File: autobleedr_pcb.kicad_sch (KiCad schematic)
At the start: 20 parts, among them J11 Conn_01x02_Pin, J13 Screw_Terminal_01x08, J7 Screw_Terminal_01x02, Q1 PMOS, Q2 IRLML2060, SW1 SW_SPST, U2 ESP32, U6 TMC2209

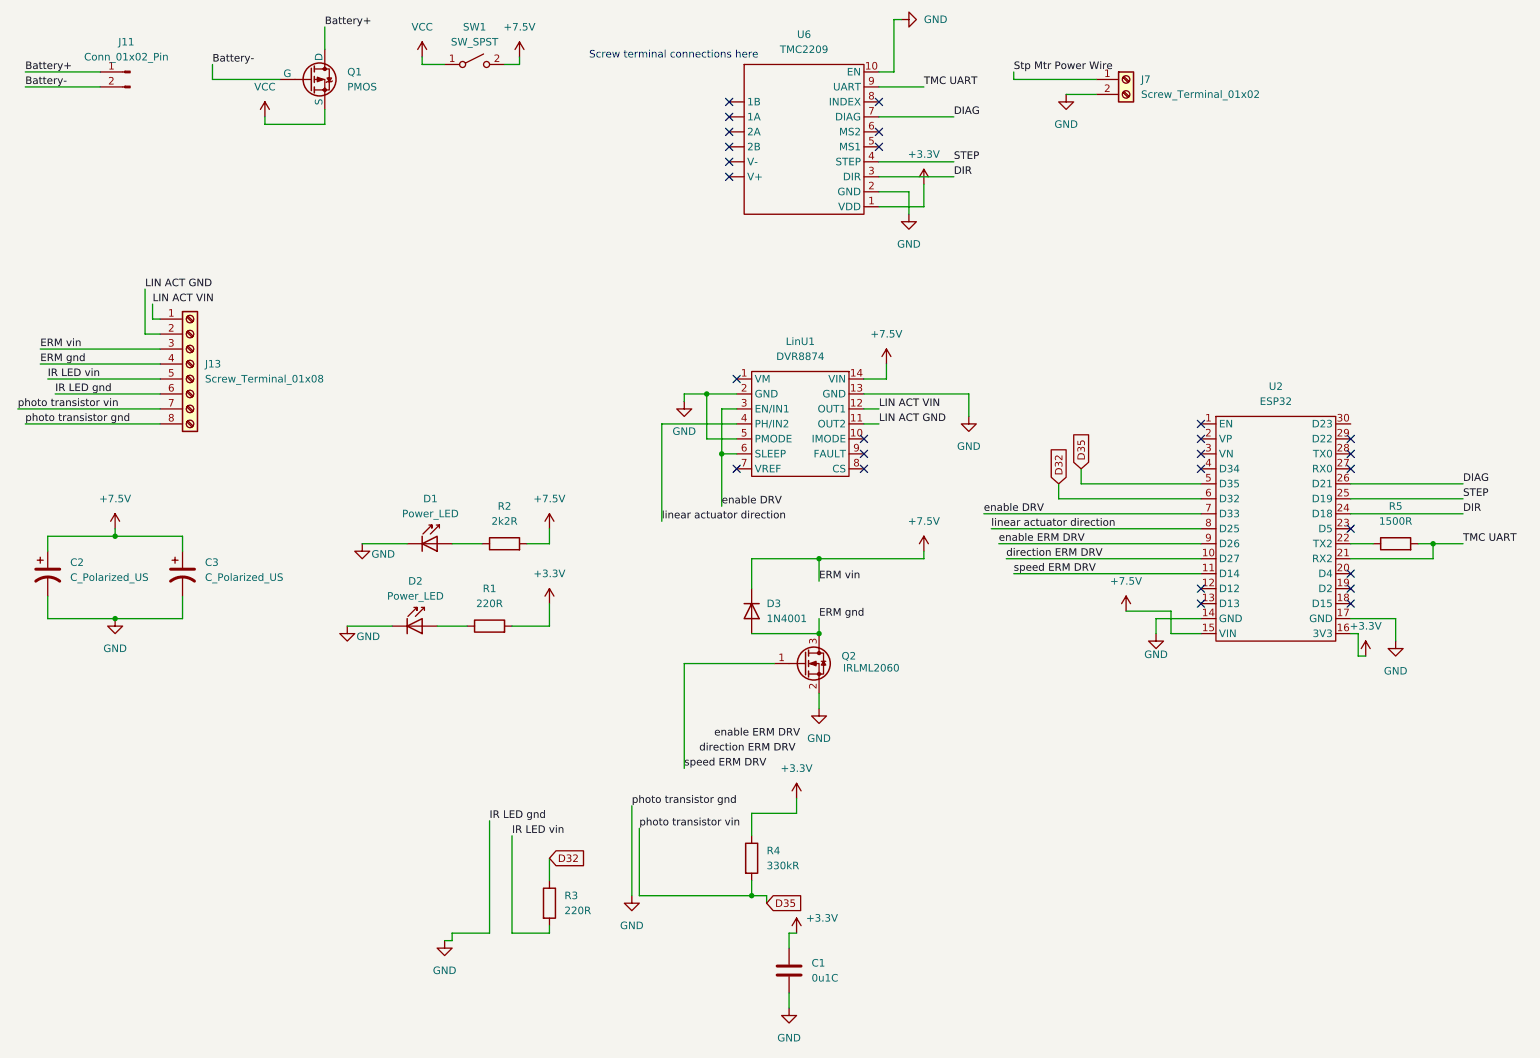
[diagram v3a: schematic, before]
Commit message: updated pcb traces with binh nmos design
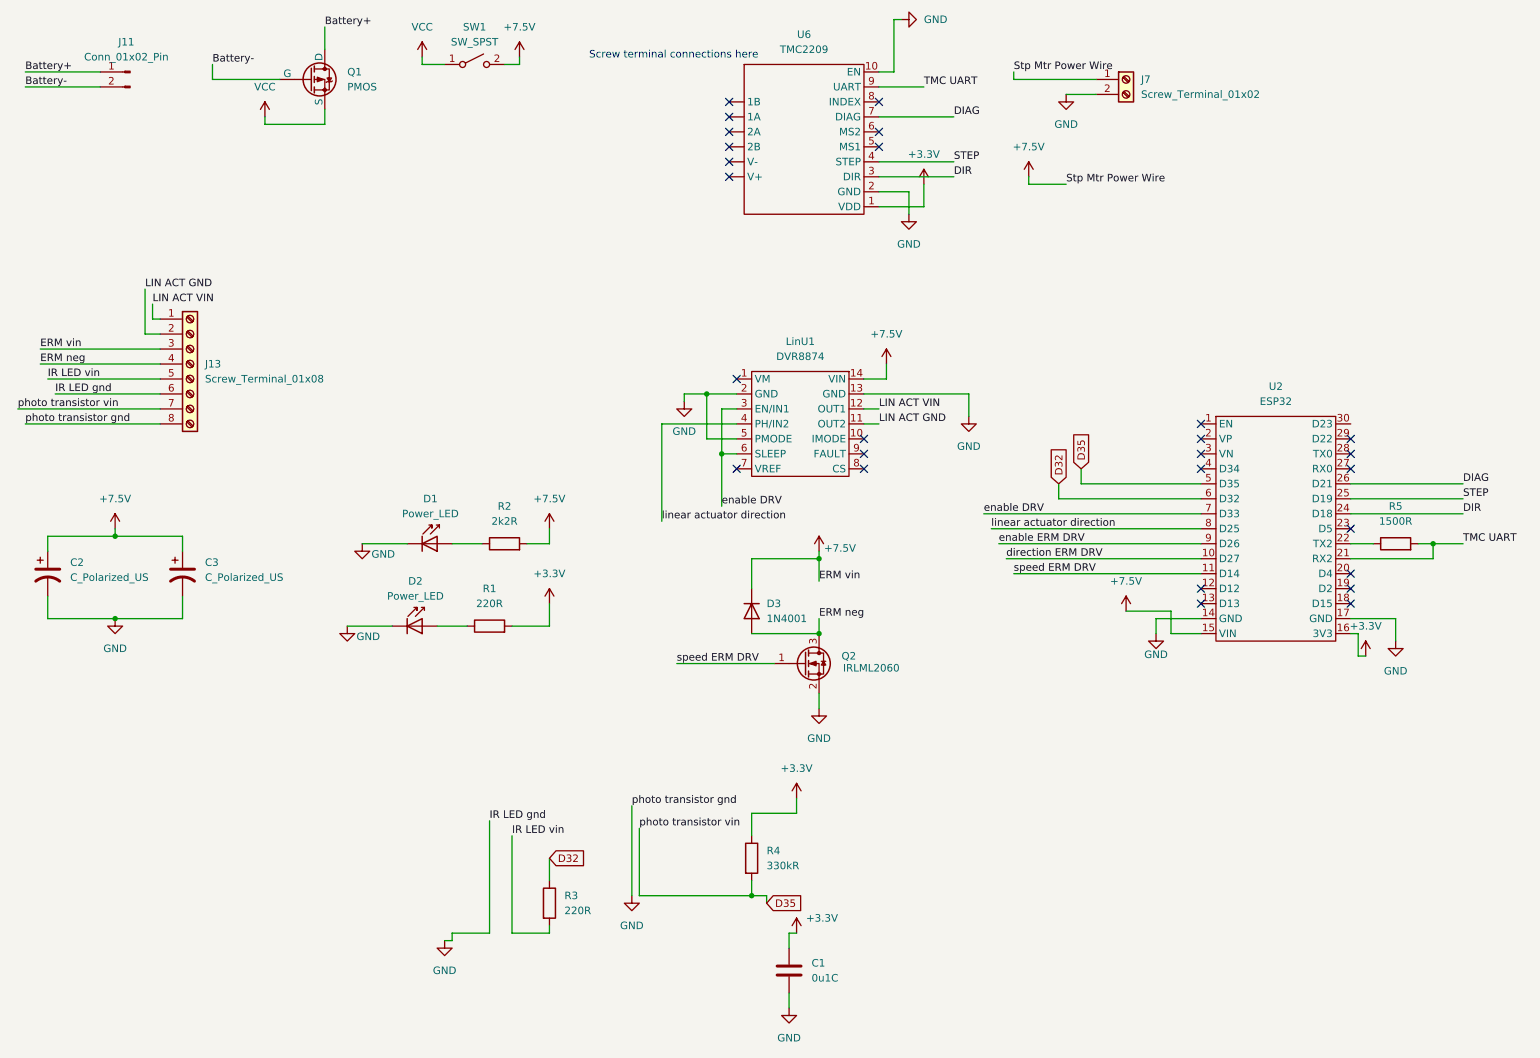
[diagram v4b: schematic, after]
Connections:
- net Stp Mtr Power Wire is gone; now on net +7.5V: J7.1 (Pin_1)
- net ERM gnd renamed ERM neg
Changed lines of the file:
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@@
 	(wire
 		(pts
+			(xy 195.58 46.99) (xy 189.23 46.99)
+		)
+		(stroke
+			(width 0)
+			(type default)
+		)
+	)
+	(wire
+		(pts
 			(xy 144.78 167.64) (xy 144.78 168.91)
 		)
@@
 	(wire
 		(pts
-			(xy 171.45 110.49) (xy 171.45 109.22)
-		)
-		(stroke
-			(width 0)
-			(type default)
-		)
-	)
-	(wire
-		(pts
-			(xy 153.67 110.49) (xy 171.45 110.49)
-		)
-		(stroke
-			(width 0)
-			(type default)
-		)
-	)
-	(wire
-		(pts
 			(xy 163.83 43.18) (xy 176.53 43.18)
 		)
@@
 	(wire
 		(pts
-			(xy 130.81 128.27) (xy 146.05 128.27)
+			(xy 129.54 128.27) (xy 146.05 128.27)
 		)
 		(stroke
@@
 	(wire
 		(pts
-			(xy 130.81 128.27) (xy 130.81 146.05)
-		)
-		(stroke
-			(width 0)
-			(type default)
-		)
-	)
-	(wire
-		(pts
 			(xy 186.69 29.21) (xy 200.66 29.21)
 		)
@@
 	(wire
 		(pts
+			(xy 189.23 46.99) (xy 189.23 45.72)
+		)
+		(stroke
+			(width 0)
+			(type default)
+		)
+	)
+	(wire
+		(pts
 			(xy 39.37 64.77) (xy 39.37 72.39)
 		)
@@
 	(wire
 		(pts
+			(xy 153.67 110.49) (xy 153.67 109.22)
+		)
+		(stroke
+			(width 0)
+			(type default)
+		)
+	)
+	(wire
+		(pts
 			(xy 148.59 184.15) (xy 148.59 186.69)
 		)
@@
 		)
 	)
-	(label "IR LED gnd"
-		(at 97.79 154.94 0)
+	(label "Stp Mtr Power Wire"
+		(at 195.58 46.99 0)
 		(effects
 			(font
@@
 		)
 	)
-	(label "direction ERM DRV"
-		(at 133.35 143.51 0)
+	(label "IR LED gnd"
+		(at 97.79 154.94 0)
 		(effects
 			(font
@@
 		)
 	)
-	(label "ERM gnd"
+	(label "ERM neg"
 		(at 21.59 77.47 0)
 		(effects
@@
 		)
 	)
-	(label "enable ERM DRV"
-		(at 135.89 140.97 0)
-		(effects
-			(font
-				(size 1.27 1.27)
-			)
-			(justify left bottom)
-		)
-	)
 	(label "Battery-"
 		(at 50.8 26.67 0)
@@
 	)
 	(label "speed ERM DRV"
-		(at 130.81 146.05 0)
+		(at 129.54 128.27 0)
 		(effects
 			(font
@@
 		)
 	)
-	(label "ERM gnd"
+	(label "ERM neg"
 		(at 153.67 120.65 0)
 		(effects
@@
 	(symbol
 		(lib_id "power:+7.5V")
-		(at 171.45 109.22 0)
+		(at 153.67 109.22 0)
 		(unit 1)
 		(exclude_from_sim no)
@@
 		(on_board yes)
 		(dnp no)
-		(fields_autoplaced yes)
 		(property "Reference" "#PWR010"
-			(at 171.45 113.03 0)
+			(at 153.67 113.03 0)
 			(effects
 				(font
@@
 		)
 		(property "Value" "+7.5V"
-			(at 171.45 104.14 0)
+			(at 157.226 108.712 0)
 			(effects
 				(font
@@
 		)
 		(property "Footprint" ""
-			(at 171.45 109.22 0)
+			(at 153.67 109.22 0)
 			(effects
 				(font
@@
 		)
 		(property "Datasheet" ""
-			(at 171.45 109.22 0)
+			(at 153.67 109.22 0)
 			(effects
 				(font
@@
 		)
 		(property "Description" "Power symbol creates a global label with name \"+7.5V\""
-			(at 171.45 109.22 0)
+			(at 153.67 109.22 0)
 			(effects
 				(font
@@
 					(unit 1)
 				)
+			)
+		)
+	)
+	(symbol
+		(lib_id "power:+7.5V")
+		(at 189.23 45.72 0)
+		(unit 1)
+		(exclude_from_sim no)
+		(in_bom yes)
+		(on_board yes)
+		(dnp no)
+		(fields_autoplaced yes)
+		(property "Reference" "#PWR020"
+			(at 189.23 49.53 0)
+			(effects
+				(font
+					(size 1.27 1.27)
+				)
+				(hide yes)
+			)
+		)
+		(property "Value" "+7.5V"
+			(at 189.23 40.64 0)
+			(effects
+				(font
+					(size 1.27 1.27)
+				)
+			)
+		)
+		(property "Footprint" ""
+			(at 189.23 45.72 0)
+			(effects
+				(font
+					(size 1.27 1.27)
+				)
+				(hide yes)
+			)
+		)
+		(property "Datasheet" ""
+			(at 189.23 45.72 0)
+			(effects
+				(font
+					(size 1.27 1.27)
+				)
+				(hide yes)
+			)
+		)
+		(property "Description" "Power symbol creates a global label with name \"+7.5V\""
+			(at 189.23 45.72 0)
+			(effects
+				(font
+					(size 1.27 1.27)
+				)
+				(hide yes)
+			)
+		)
+		(pin "1"
+		)
+		(instances
+			(project ""
+				(path "/1cb070e6-4268-4590-be3a-70f1be021dfd"
+					(reference "#PWR020")
+					(unit 1)
+				)

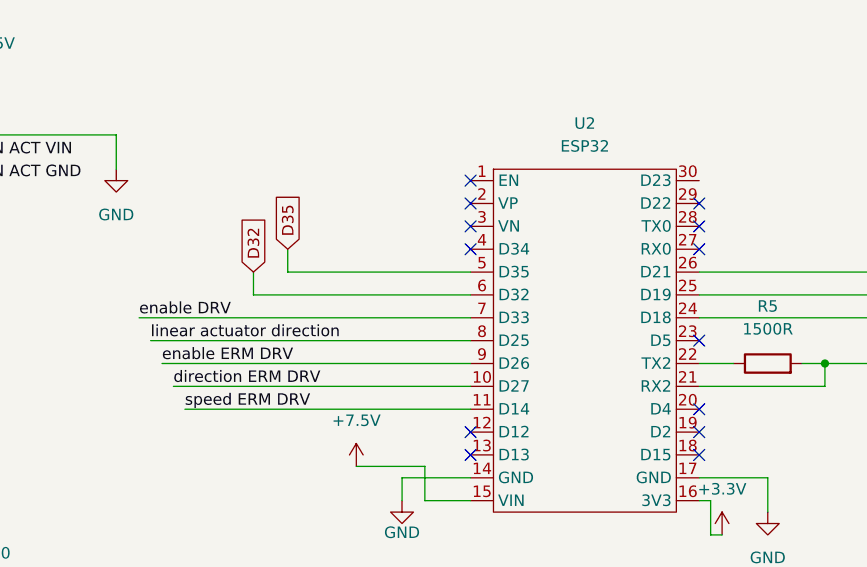
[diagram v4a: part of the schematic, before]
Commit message: Added another rendition to the pcb layout
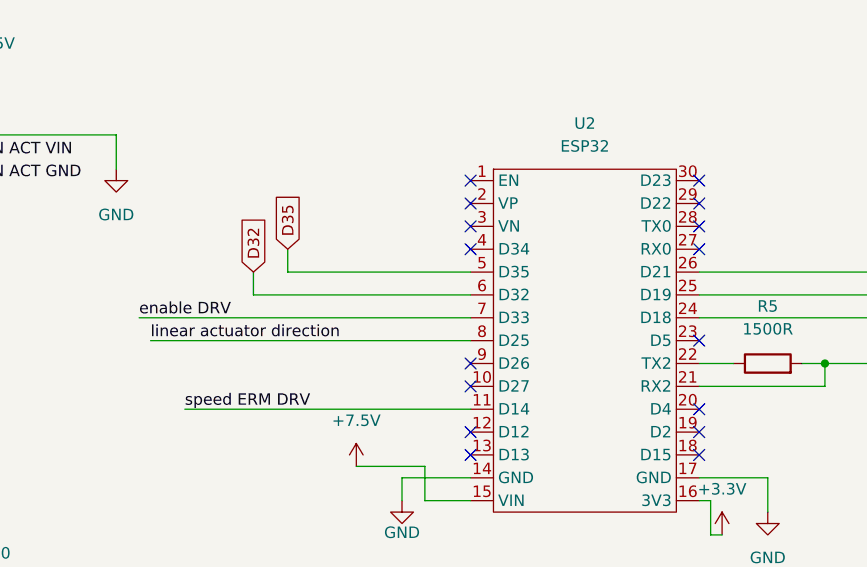
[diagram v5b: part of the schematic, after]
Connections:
- net direction ERM DRV: no longer names the net of U2.10 (D27)
- net enable ERM DRV: no longer names the net of U2.9 (D26)
- no-connect marks 27 -> 30
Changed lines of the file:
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@@
+	)
+	(no_connect
+		(at 218.44 110.49)
 	)
 	(no_connect
@@
 	)
 	(no_connect
+		(at 218.44 107.95)
+	)
+	(no_connect
 		(at 218.44 118.11)
 	)
@@
 	)
 	(no_connect
+		(at 243.84 87.63)
+	)
+	(no_connect
 		(at 161.29 90.17)
 	)
@@
 	(wire
 		(pts
-			(xy 184.15 107.95) (xy 218.44 107.95)
-		)
-		(stroke
-			(width 0)
-			(type default)
-		)
-	)
-	(wire
-		(pts
 			(xy 69.85 36.83) (xy 69.85 34.29)
 		)
@@
 		(pts
 			(xy 19.05 27.94) (xy 31.75 27.94)
-		)
-		(stroke
-			(width 0)
-			(type default)
-		)
-	)
-	(wire
-		(pts
-			(xy 185.42 110.49) (xy 218.44 110.49)
 		)
 		(stroke
@@
 		)
 	)
-	(label "direction ERM DRV"
-		(at 185.42 110.49 0)
-		(effects
-			(font
-				(size 1.27 1.27)
-			)
-			(justify left bottom)
-		)
-	)
 	(label "Battery-"
 		(at 19.05 30.48 0)
@@
 		(effects
 			(font
-				(size 1.27 1.27)
-			)
-			(justify left bottom)
-		)
-	)
-	(label "enable ERM DRV"
-		(at 184.15 107.95 0)
-		(effects
-			(font

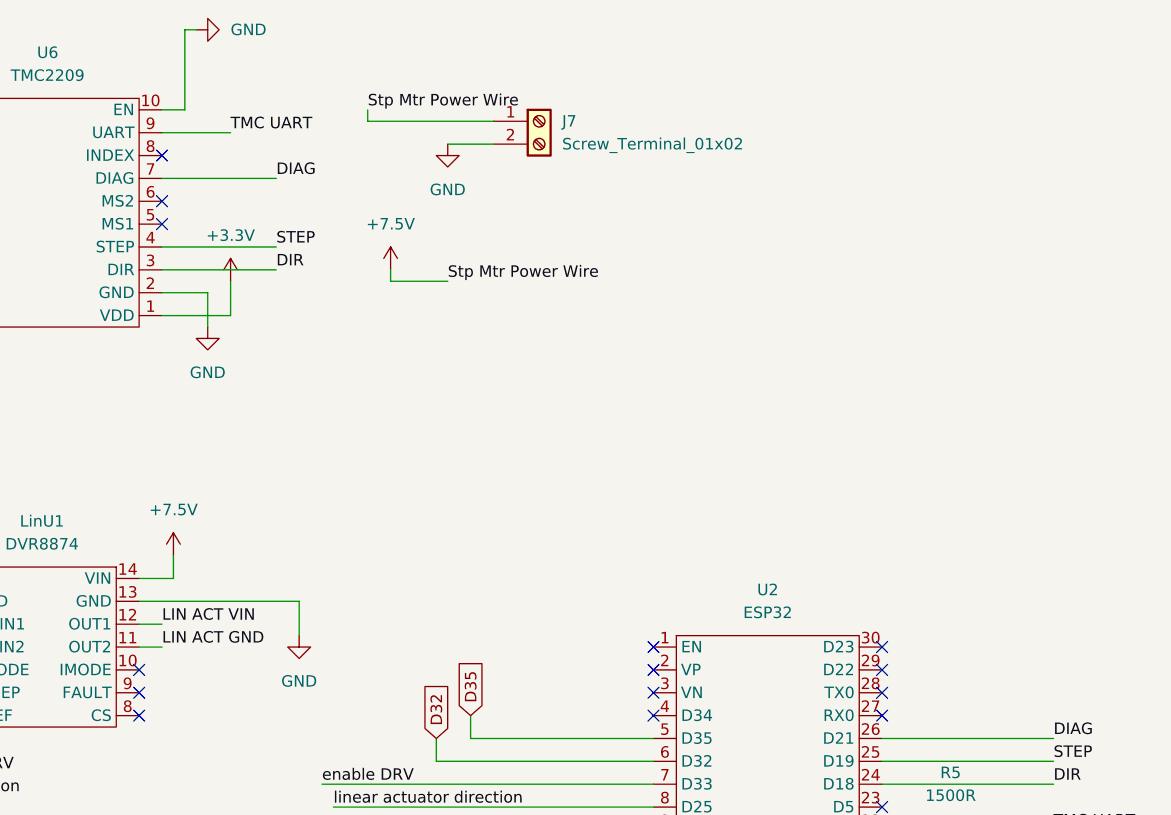
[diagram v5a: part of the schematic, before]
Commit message: Added EN pin and c1
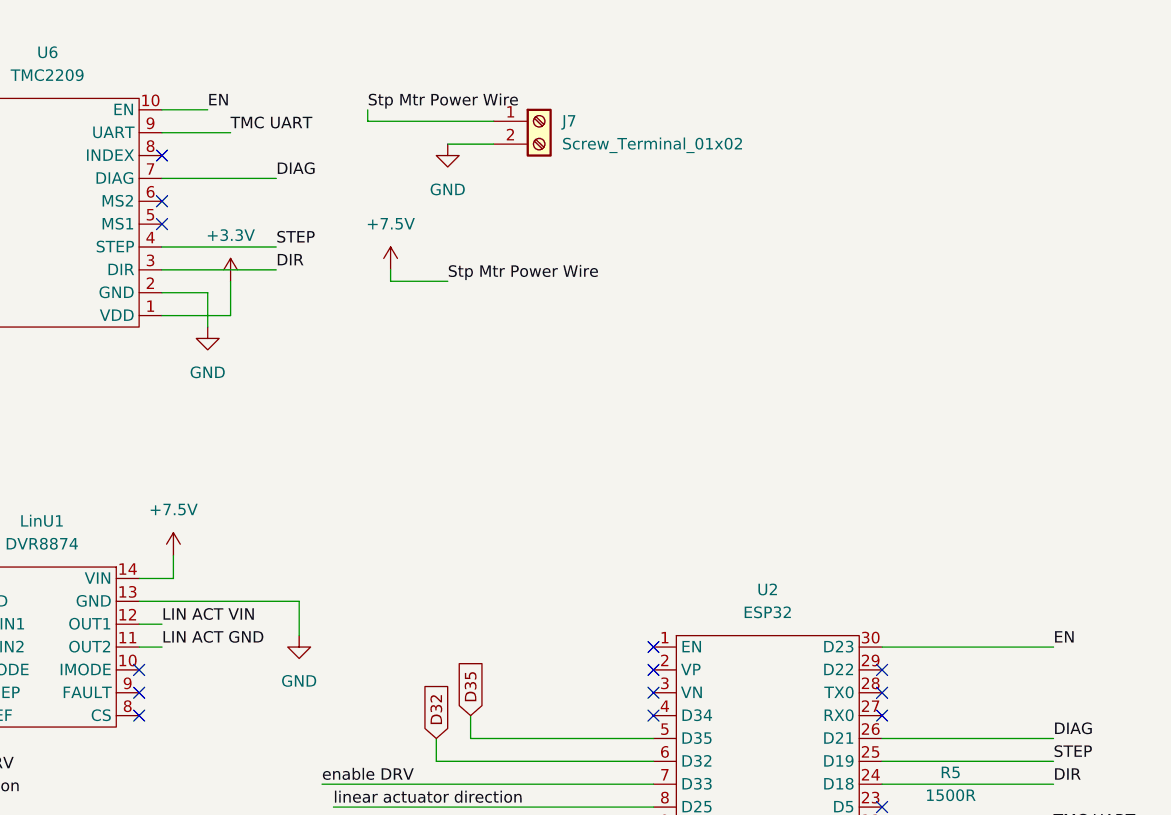
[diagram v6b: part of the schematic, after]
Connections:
- net GND: no longer U6.10 (EN)
- net EN: now reaches U2.30 (D23)
- net EN: now also U6.10 (EN)
- no-connect marks 30 -> 29
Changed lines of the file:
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@@
-	)
-	(no_connect
-		(at 243.84 87.63)
 	)
 	(no_connect
@@
 	(wire
 		(pts
-			(xy 166.37 19.05) (xy 167.64 19.05)
-		)
-		(stroke
-			(width 0)
-			(type default)
-		)
-	)
-	(wire
-		(pts
 			(xy 161.29 87.63) (xy 163.83 87.63)
 		)
@@
 	(wire
 		(pts
+			(xy 243.84 87.63) (xy 262.89 87.63)
+		)
+		(stroke
+			(width 0)
+			(type default)
+		)
+	)
+	(wire
+		(pts
 			(xy 213.36 119.38) (xy 213.36 123.19)
 		)
@@
 	(wire
 		(pts
-			(xy 166.37 27.94) (xy 166.37 19.05)
-		)
-		(stroke
-			(width 0)
-			(type default)
-		)
-	)
-	(wire
-		(pts
 			(xy 142.24 123.19) (xy 153.67 123.19)
 		)
@@
 	(wire
 		(pts
-			(xy 163.83 27.94) (xy 166.37 27.94)
+			(xy 163.83 27.94) (xy 168.91 27.94)
 		)
 		(stroke
@@
 		)
 	)
+	(label "EN"
+		(at 262.89 87.63 0)
+		(effects
+			(font
+				(size 1.27 1.27)
+			)
+			(justify left bottom)
+		)
+	)
 	(label "ERM vin"
 		(at 21.59 74.93 0)
@@
 	(label "DIR"
 		(at 176.53 45.72 0)
+		(effects
+			(font
+				(size 1.27 1.27)
+			)
+			(justify left bottom)
+		)
+	)
+	(label "EN"
+		(at 168.91 27.94 0)
 		(effects
 			(font
@@
 					(unit 1)
 				)
-			)
-		)
-	)
-	(symbol
-		(lib_id "power:GND")
-		(at 167.64 19.05 90)
-		(unit 1)
-		(exclude_from_sim no)
-		(in_bom yes)
-		(on_board yes)
-		(dnp no)
-		(fields_autoplaced yes)
-		(property "Reference" "#PWR040"
-			(at 173.99 19.05 0)
-			(effects
-				(font
-					(size 1.27 1.27)
-				)
-				(hide yes)
-			)
-		)
-		(property "Value" "GND"
-			(at 171.45 19.0499 90)
-			(effects
-				(font
-					(size 1.27 1.27)
-				)
-				(justify right)
-			)
-		)
-		(property "Footprint" ""
-			(at 167.64 19.05 0)
-			(effects
-				(font
-					(size 1.27 1.27)
-				)
-				(hide yes)
-			)
-		)
-		(property "Datasheet" ""
-			(at 167.64 19.05 0)
-			(effects
-				(font
-					(size 1.27 1.27)
-				)
-				(hide yes)
-			)
-		)
-		(property "Description" "Power symbol creates a global label with name \"GND\" , ground"
-			(at 167.64 19.05 0)
-			(effects
-				(font
-					(size 1.27 1.27)
-				)
-				(hide yes)
-			)
-		)
-		(pin "1"
-		)
-		(instances
-			(project "autobleedr_pcb"
-				(path "/1cb070e6-4268-4590-be3a-70f1be021dfd"
-					(reference "#PWR040")
-					(unit 1)
-				)

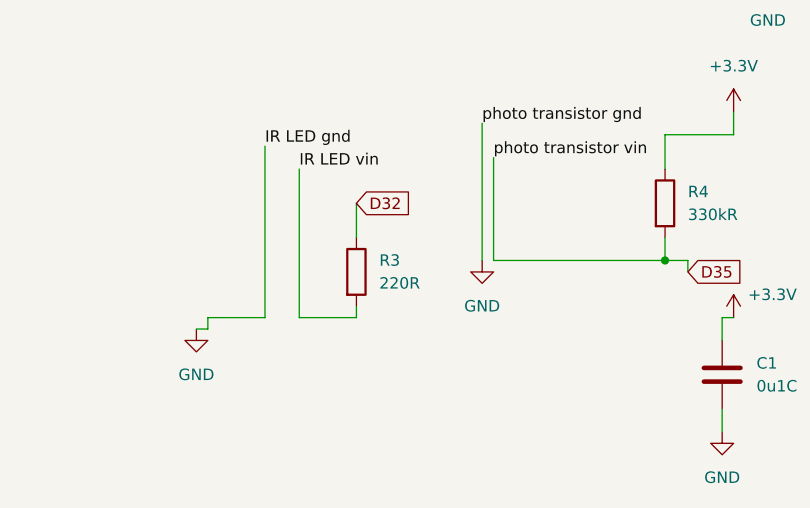
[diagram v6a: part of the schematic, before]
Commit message: Update bubble circuit
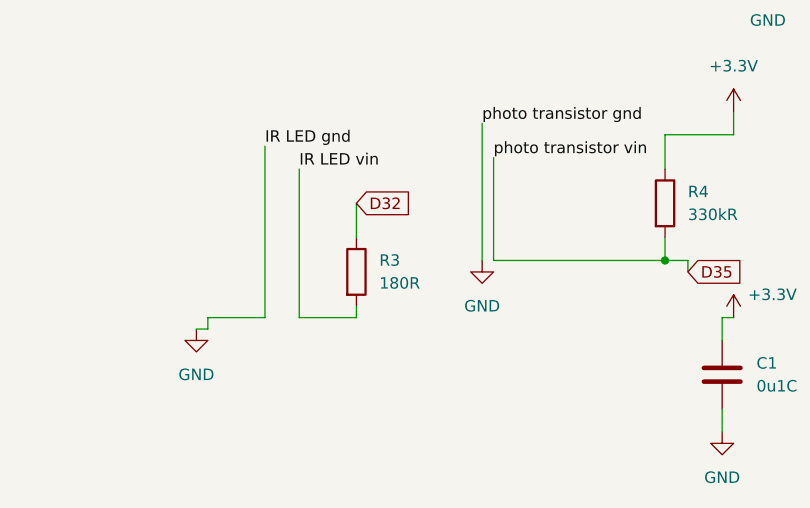
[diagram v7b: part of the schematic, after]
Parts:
- R3: value 220R -> 180R
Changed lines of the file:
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@@
 			)
 		)
-		(property "Value" "220R"
+		(property "Value" "180R"
 			(at 110.49 170.1799 0)
 			(effects
